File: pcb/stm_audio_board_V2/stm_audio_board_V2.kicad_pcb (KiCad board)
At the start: 4 copper layers, 158 parts, among them J1 Power conn, J10 Conn_01x03_taptempo, J11 SPI, J2 STlink, J3 Audio_sig, J4 Conn_01x10_pots_internal, J6 Conn_01x03_pot_ext, SW1 SW_SPST, U1 STM32H730VBTx, U1 STM32H747IGTx, U2 OP275, U3 STM32H747AIIx, U4 OP275, U5 AMS1117-3.3, U8 L78M09CDT, U9 LF33_TO252, Y1 Crystal_GND24, Y2 X1E0000210132

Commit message: pinsetup ready
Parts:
- removed C13: 2.2uF, Capacitor_SMD:C_0805_2012Metric_Pad1.18x1.45mm_HandSolder
- removed FB1, FB2: FerriteBead, Resistor_SMD:R_0603_1608Metric_Pad0.98x0.95mm_HandSolder
- removed R2: 10k, Resistor_SMD:R_0805_2012Metric_Pad1.20x1.40mm_HandSolder
- removed the U1 at (214.0, 68.3)
- added C103: 2u2F, Capacitor_SMD:C_0603_1608Metric_Pad1.08x0.95mm_HandSolder, F.Cu at (136.3, 102.2)
- added C104: 2u2F, Capacitor_SMD:C_0603_1608Metric_Pad1.08x0.95mm_HandSolder, F.Cu at (136.3, 104.7)
- added C105: 2u2F, Capacitor_SMD:C_0603_1608Metric_Pad1.08x0.95mm_HandSolder, F.Cu at (136.3, 107.3)
- added C3: 10uF 50V ceramic, Capacitor_SMD:C_0603_1608Metric_Pad1.08x0.95mm_HandSolder, F.Cu at (136.3, 92.2)
- added C4: 22uF 50V ceramic, Capacitor_SMD:C_0603_1608Metric_Pad1.08x0.95mm_HandSolder, F.Cu at (136.3, 94.7)
- added C69: 2u2F, Capacitor_SMD:C_0603_1608Metric_Pad1.08x0.95mm_HandSolder, F.Cu at (136.3, 99.7)
- added D1: 1N4148, Diode_THT:D_DO-35_SOD27_P7.62mm_Horizontal, F.Cu at (140.1, 101.0)
- added D2: 1N4148, Diode_THT:D_DO-35_SOD27_P7.62mm_Horizontal, F.Cu at (140.1, 104.5)
- added FB3: TDK MMZ1608R601ATD25 DB, Resistor_SMD:R_0603_1608Metric_Pad0.98x0.95mm_HandSolder, F.Cu at (136.3, 109.8)
- added FB4: TDK MMZ1608R601ATD25 DB, Resistor_SMD:R_0603_1608Metric_Pad0.98x0.95mm_HandSolder, F.Cu at (136.3, 112.3)
- added J5: Conn_01x10_display TODO, Connector_PinHeader_2.54mm:PinHeader_1x10_P2.54mm_Vertical, F.Cu at (129.8, 93.3)
- C15: value 2.2uF -> 2u2F; footprint Capacitor_SMD:C_0805_2012Metric_Pad1.18x1.45mm_HandSolder -> Capacitor_SMD:C_0603_1608Metric_Pad1.08x0.95mm_HandSolder; moved to F.Cu
- U3: value STM32H747AIIx -> MP-K7805-500R3; footprint Package_BGA:UFBGA-169_7x7mm_Layout13x13_P0.5mm -> Package_TO_SOT_THT:TO-220-3_Vertical
- U5: value AMS1117-3.3 -> MIC2920A-3.3WS-TR; footprint Package_TO_SOT_SMD:SOT-223-3_TabPin2 -> Package_TO_SOT_SMD:SOT-223
- U8: value L78M09CDT -> ROHM BA09CC0FP-E2; footprint Package_TO_SOT_SMD:TO-252-2 -> Package_TO_SOT_SMD:TO-252-3_TabPin2
- U9: value LF33_TO252 -> MIC2920A-3.3WS-TR; footprint Package_TO_SOT_SMD:TO-252-2 -> Package_TO_SOT_SMD:SOT-223
- moved C15 85.9 mm to (136.3, 97.2)
- moved U3 52.5 mm to (141.8, 110.2)
- moved U5 48.3 mm to (143.4, 95.1)
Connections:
- C102 pad 1: PWR_INPUT_12V-18V -> 5V
- C15 pad 1: Net-(C15-Pad1) -> 5V
- C27 pad 1: +9V -> Net-(D2-K)
- C28 pad 1: +9V -> Net-(D2-K)
- C48 pad 1: PWR_INPUT_12V-18V -> Net-(D3-K)
- C70 pad 1: Net-(D5-K) -> 5V
- D5 pad 1: Net-(D5-K) -> 5V
- U1 pad 132: SWDIO -> unconnected-(U1-PA13-Pad132)
- U1 pad 138: SWCLK -> unconnected-(U1-PA14-Pad138)
- U1 pad 140: unconnected-(U1-PC10-Pad140) -> AD1939_SPI3_CLK
- U1 pad 141: unconnected-(U1-PC11-Pad141) -> AD1939_SPI3_MISO
- U1 pad 35: unconnected-(U1-PC1-Pad35) -> AD1939_I2S2_SDO
- U1 pad 46: ADC_EN -> unconnected-(U1-PA3-Pad46)
- U1 pad 49: DAC_EN -> AD1939_I2S1_WS
- U1 pad 50: CLK -> AD1939_I2S1_CK
- U1 pad 51: MISO -> AD1939_I2S1_SDI
- U1 pad 52: MOSI -> unconnected-(U1-PA7-Pad52)
- U1 pad 57: unconnected-(U1-PB2-Pad57) -> AD1939_SPI3_MOSI
- U1 pad 78: unconnected-(U1-PB10-Pad78) -> AD1939_I2S2_CK
- U1 pad 85: unconnected-(U1-PB12-Pad85) -> AD1939_I2S2_WS
- U11 pad 20: unconnected-(U11A-DSDATA1-Pad20) -> AD1939_I2S2_SDO
- U11 pad 21: unconnected-(U11A-DBCLK-Pad21) -> AD1939_I2S2_CK
- U11 pad 22: unconnected-(U11A-DLRCLK-Pad22) -> AD1939_I2S2_WS
- U11 pad 27: unconnected-(U11A-ASDATA1-Pad27) -> AD1939_I2S1_SDI
- U11 pad 28: unconnected-(U11A-ABCLK-Pad28) -> AD1939_I2S1_CK
- U11 pad 29: unconnected-(U11A-ALRCLK-Pad29) -> AD1939_I2S1_WS
- U11 pad 30: MOSI -> AD1939_SPI3_MOSI
- U11 pad 31: MISO -> AD1939_SPI3_MISO
- U11 pad 34: CLK -> AD1939_SPI3_CLK
- U11 pad 35: DAC_EN -> AD1939_SPI_CS
- U11 pad 36: unconnected-(U11A-OL1P-Pad36) -> DAC1R
- U11 pad 37: unconnected-(U11A-OL1N-Pad37) -> DAC1L
- U11 pad 38: unconnected-(U11A-OR1P-Pad38) -> DAC2R
- U11 pad 39: unconnected-(U11A-OR1N-Pad39) -> DAC2L
- U11 pad 40: DAC1R -> unconnected-(U11A-OL2P-Pad40)
- U11 pad 41: DAC1L -> unconnected-(U11A-OL2N-Pad41)
- U11 pad 42: DAC2R -> unconnected-(U11A-OR2P-Pad42)
- U11 pad 43: DAC2L -> unconnected-(U11A-OR2N-Pad43)
- U5 pad 1: GND -> Net-(D2-K)
- U5 pad 2: +3.3VA -> GND
- U5 pad 3: +9V -> +3.3VA
- U9 pad 1: Net-(D5-K) -> 5V
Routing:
- net DAC_EN: track 17.3 -> 0.00 mm
- net AD1939_SPI_CS: track 0.00 -> 17.3 mm
- net Net-(D5-K): track 17.1 -> 0.00 mm
- net 5V: track 0.00 -> 17.1 mm
- net (no net): track 0.00 -> 8.78 mm, vias 0 -> 1
- net Net-(C15-Pad1): track 4.45 -> 0.00 mm, vias 1 -> 0
- net Net-(C13-Pad1): track 4.33 -> 0.00 mm

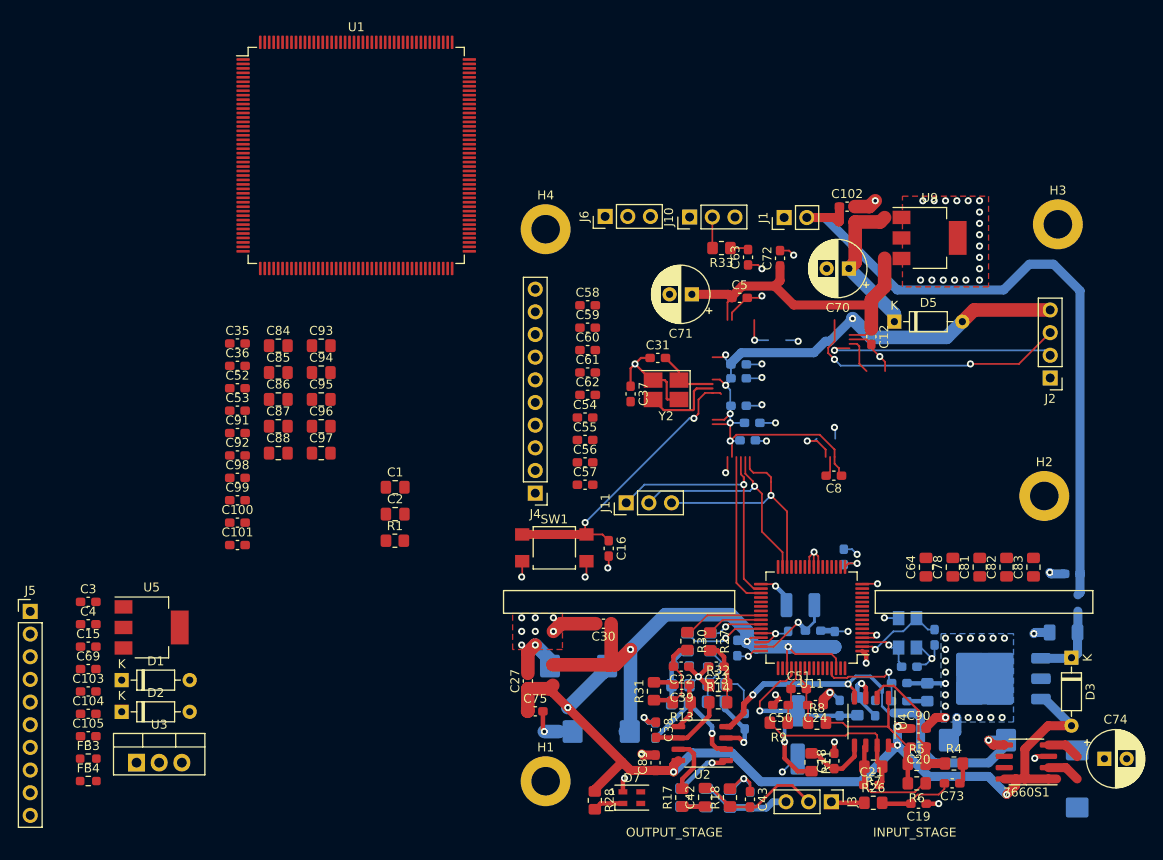
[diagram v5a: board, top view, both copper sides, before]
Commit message: Capacitor types are choosen, schematic updated, unused capacitors deleted. Connectors need to be connected to the mcu and its finished
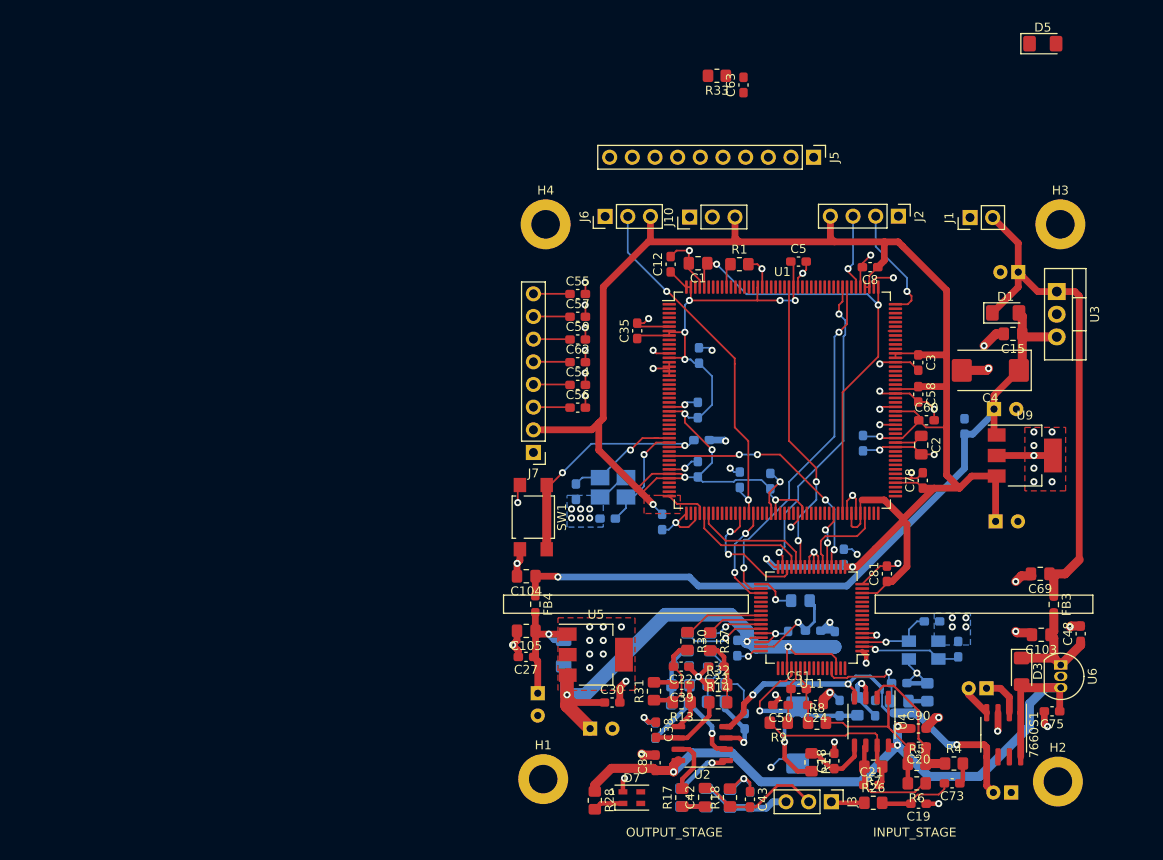
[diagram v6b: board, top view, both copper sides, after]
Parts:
- removed C100, C101, C36, C52, C53, C72, C91, C92, C98, C99: 100nF, Capacitor_SMD:C_0603_1608Metric_Pad1.08x0.95mm_HandSolder
- removed C49: 100uF, Capacitor_SMD:C_1206_3216Metric_Pad1.33x1.80mm_HandSolder
- removed C74: 47uf, Capacitor_THT:CP_Radial_D6.3mm_P2.50mm
- removed C82, C83, C84, C85, C86, C87, C88, C93, C94, C95, C96, C97: 47uF, Capacitor_SMD:C_0805_2012Metric_Pad1.18x1.45mm_HandSolder
- removed J11: SPI, Connector_PinHeader_2.54mm:PinHeader_1x03_P2.54mm_Vertical
- removed J4: Conn_01x10_pots_internal, Connector_PinHeader_2.54mm:PinHeader_1x10_P2.54mm_Vertical
- removed U8: ROHM BA09CC0FP-E2, Package_TO_SOT_SMD:TO-252-3_TabPin2
- added C13: 22uF 50V poly, Capacitor_THT:CP_Radial_D5.0mm_P2.00mm, B.Cu at (240.6, 55.2)
- added J7: Conn_01x8_pots_internal, Connector_PinHeader_2.54mm:PinHeader_1x08_P2.54mm_Vertical, F.Cu at (186.2, 75.5)
- added U6: L7809, Package_TO_SOT_THT:TO-92_Inline, F.Cu at (245.3, 99.3)
- C102, C16, C31, C37, C61, C70, C71, Y2: moved to B.Cu
- C103, C104, C105, C15, C67, C69: footprint Capacitor_SMD:C_0603_1608Metric_Pad1.08x0.95mm_HandSolder -> Capacitor_SMD:C_0805_2012Metric_Pad1.18x1.45mm_HandSolder
- C26: value 100uF -> 100uF tantal; footprint Capacitor_SMD:CP_Elec_6.3x7.7 -> Capacitor_Tantalum_SMD:CP_EIA-7343-31_Kemet-D_Pad2.25x2.55mm_HandSolder
- C28: footprint Capacitor_Tantalum_SMD:CP_EIA-7343-31_Kemet-D_Pad2.25x2.55mm_HandSolder -> Capacitor_THT:CP_Radial_D6.3mm_P2.50mm
- C29: value 1uF -> 47uF; footprint Capacitor_Tantalum_SMD:CP_EIA-7343-31_Kemet-D_Pad2.25x2.55mm_HandSolder -> Capacitor_THT:CP_Radial_D6.3mm_P2.50mm
- C3: value 10uF 50V ceramic -> 100nF
- C4: value 22uF 50V ceramic -> 22uF tantal; footprint Capacitor_SMD:C_0603_1608Metric_Pad1.08x0.95mm_HandSolder -> Capacitor_Tantalum_SMD:CP_EIA-7343-31_Kemet-D_Pad2.25x2.55mm_HandSolder
- C48: moved to F.Cu
- C64: value 47uF -> 100nF; footprint Capacitor_SMD:C_0805_2012Metric_Pad1.18x1.45mm_HandSolder -> Capacitor_SMD:C_0603_1608Metric_Pad1.08x0.95mm_HandSolder; moved to B.Cu
- C76, C77: footprint Capacitor_Tantalum_SMD:CP_EIA-7343-31_Kemet-D_Pad2.25x2.55mm_HandSolder -> Capacitor_THT:CP_Radial_D5.0mm_P2.00mm
- C78, C81: value 47uF -> 100nF; footprint Capacitor_SMD:C_0805_2012Metric_Pad1.18x1.45mm_HandSolder -> Capacitor_SMD:C_0603_1608Metric_Pad1.08x0.95mm_HandSolder
- C80: value 10uF -> 10uF tantal; footprint Capacitor_SMD:C_1210_3225Metric_Pad1.33x2.70mm_HandSolder -> Capacitor_SMD:C_0805_2012Metric_Pad1.18x1.45mm_HandSolder
- D1, D3, D5: footprint Diode_THT:D_DO-35_SOD27_P7.62mm_Horizontal -> Diode_SMD:D_1206_3216Metric_Pad1.42x1.75mm_HandSolder
- D2: footprint Diode_THT:D_DO-35_SOD27_P7.62mm_Horizontal -> Diode_SMD:D_1206_3216Metric_Pad1.42x1.75mm_HandSolder; moved to B.Cu
- J5: value Conn_01x10_display TODO -> Conn_01x10_display
- U5, U9: footprint Package_TO_SOT_SMD:SOT-223 -> Package_TO_SOT_SMD:SOT-223-3_TabPin2
- moved U3 115.9 mm to (244.9, 57.4), turned to -90 degrees
- moved FB3 109.6 mm to (244.5, 92.5), turned to -90 degrees
- moved C15 109.4 mm to (240.0, 62.2), turned to 180 degrees
- moved D1 107.3 mm to (239.2, 59.8)
- moved C69 107.2 mm to (243.0, 89.1), turned to 180 degrees
- moved C103 107.0 mm to (243.1, 95.9), turned to 180 degrees
- moved C4 105.0 mm to (237.4, 66.3), turned to 180 degrees
- moved J5 101.5 mm to (217.6, 42.4), turned to -90 degrees
- moved C3 96.8 mm to (229.4, 65.4), turned to -90 degrees
- moved C2 59.5 mm to (229.7, 74.6), turned to -90 degrees
- moved C75 57.9 mm to (244.3, 104.5), turned to 180 degrees
- moved U1 55.1 mm to (214.1, 69.6)
- moved FB4 53.9 mm to (186.4, 92.5), turned to -90 degrees
- moved C104 51.5 mm to (185.4, 89.3), turned to 180 degrees
- moved C105 50.5 mm to (185.4, 95.5), turned to 180 degrees
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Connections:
- C3 pad 1: PWR_INPUT_12V-18V -> +3.3V
- C35 pad 1: +3.3VA -> +3.3V
- C58 pad 1: POT7 -> +3.3V
- C60 pad 1: POT8 -> +3.3V
- C64 pad 1: +3.3VA -> +3.3V
- C78 pad 1: +3.3VA -> +3.3V
- C81 pad 1: +3.3VA -> +3.3V
- J10 pad 3: VDD -> +3.3V
- J5 pad 1: unconnected-(J5-Pin_1-Pad1) -> +3.3V
- J5 pad 10: unconnected-(J5-Pin_10-Pad10) -> TOUCH_IRQ
- J5 pad 2: unconnected-(J5-Pin_2-Pad2) -> GND
- J5 pad 3: unconnected-(J5-Pin_3-Pad3) -> DISPLAY_CS
- J5 pad 4: unconnected-(J5-Pin_4-Pad4) -> DISPLAY_RST
- J5 pad 5: unconnected-(J5-Pin_5-Pad5) -> DISPLAY_DC
- J5 pad 6: unconnected-(J5-Pin_6-Pad6) -> DISPLAY_MOSI
- J5 pad 7: unconnected-(J5-Pin_7-Pad7) -> DISPLAY_SCK
- J5 pad 8: unconnected-(J5-Pin_8-Pad8) -> DISPLAY_MISO
- J5 pad 9: unconnected-(J5-Pin_9-Pad9) -> TOUCH_CS
- J6 pad 3: VDD -> +3.3V
- U1 pad 1: unconnected-(U1-PE2-Pad1) -> DISPLAY_SCK
- U1 pad 118: unconnected-(U1-PG8-Pad118) -> EXT_INT_BUTTON
- U1 pad 132: unconnected-(U1-PA13-Pad132) -> SWDIO
- U1 pad 138: unconnected-(U1-PA14-Pad138) -> SWCLK
- U1 pad 153: unconnected-(U1-PG9-Pad153) -> AD1939_I2S1_SDI
- U1 pad 169: unconnected-(U1-PB9-Pad169) -> TOUCH_IRQ
- U1 pad 170: unconnected-(U1-PE0-Pad170) -> DISPLAY_RST
- U1 pad 171: unconnected-(U1-PE1-Pad171) -> TOUCH_CS
- U1 pad 2: unconnected-(U1-PE3-Pad2) -> DISPLAY_CS
- U1 pad 3: unconnected-(U1-PE4-Pad3) -> DISPLAY_DC
- U1 pad 34: unconnected-(U1-PC0-Pad34) -> POT4
- U1 pad 4: unconnected-(U1-PE5-Pad4) -> DISPLAY_MISO
- U1 pad 5: unconnected-(U1-PE6-Pad5) -> DISPLAY_MOSI
- U1 pad 51: AD1939_I2S1_SDI -> POT1
- U1 pad 52: unconnected-(U1-PA7-Pad52) -> POT2
- U1 pad 54: unconnected-(U1-PC5-Pad54) -> POT5
- U1 pad 56: unconnected-(U1-PB1-Pad56) -> POT3
- U1 pad 58: unconnected-(U1-PF11-Pad58) -> POT6
- U1 pad 59: unconnected-(U1-PF12-Pad59) -> POT_EXT
- U1 pad 60: unconnected-(U1-PF13-Pad60) -> AD1939_SPI_CS
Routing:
- net +3.3V: track 119.5 -> 302.8 mm, vias 7 -> 13
- net 5V: track 17.1 -> 84.1 mm, vias 0 -> 1
- net GND: track 152.7 -> 215.0 mm, vias 86 -> 88
- net Net-(C1-Pad1): track 0.00 -> 50.9 mm, vias 0 -> 2
- net POT_EXT: track 0.00 -> 40.8 mm, vias 0 -> 2
- net AD1939_SPI3_CLK: track 0.00 -> 40.3 mm, vias 0 -> 2
- net AD1939_SPI3_MISO: track 0.00 -> 35.0 mm, vias 0 -> 2
- net AD1939_I2S1_SDI: track 0.00 -> 33.6 mm, vias 0 -> 2
- net CLK: track 31.0 -> 0.00 mm, vias 1 -> 0
- net AD1939_I2S2_SDO: track 0.00 -> 27.7 mm, vias 0 -> 4
- net MISO: track 26.7 -> 0.00 mm, vias 1 -> 0
- net MOSI: track 26.4 -> 0.00 mm, vias 1 -> 0
- net SWCLK: track 31.0 -> 8.54 mm, vias 2 -> 1
- net +9V: track 106.8 -> 86.5 mm, vias 5 -> 3
- net PWR_INPUT_12V-18V: track 76.1 -> 57.3 mm
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- added copper zone on F.Cu, net +3.3V
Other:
- board text removed: "U8"

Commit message: pcb seems to be finished drc error: 0
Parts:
- removed J10: Conn_01x03_taptempo, Connector_PinHeader_2.54mm:PinHeader_1x03_P2.54mm_Vertical
- added J4: Conn_01x01_taptempo, Connector_PinHeader_2.54mm:PinHeader_1x01_P2.54mm_Vertical, F.Cu at (232.5, 49.1)
- C31, C37, Y2: moved to F.Cu
- C54, C55, C56, C57, C59, C62, C63, R33: moved to B.Cu
- moved D5 45.8 mm to (234.9, 74.7), turned to -90 degrees
- moved R33 36.8 mm to (222.7, 66.4)
- moved C63 36.5 mm to (222.7, 68.3), turned to 180 degrees
- moved J6 36.5 mm to (186.2, 84.6), turned to 180 degrees
- moved J5 25.8 mm to (192.7, 49.0), turned to 90 degrees
- moved C31 10.1 mm to (197.7, 72.2)
- moved SW1 9.21 mm to (195.0, 85.6), turned to 0 degrees
- moved C37 7.97 mm to (197.7, 75.5), turned to -90 degrees
- moved C61 7.89 mm to (207.3, 70.9)
- moved Y2 5.66 mm to (194.5, 73.7), turned to -90 degrees
- moved J1 2.03 mm to (237.2, 49.1)
- moved C104 1.02 mm to (186.4, 89.3)
- moved C54 1.02 mm to (190.2, 67.9)
- moved C56 1.02 mm to (190.2, 70.4)
- moved C59 1.02 mm to (190.2, 62.8)
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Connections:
- U1 pad 21: unconnected-(U1-PF3-Pad21) -> POT1
- U1 pad 23: unconnected-(U1-PF5-Pad23) -> POT2
- U1 pad 26: unconnected-(U1-PF6-Pad26) -> POT3
- U1 pad 27: unconnected-(U1-PF7-Pad27) -> POT4
- U1 pad 28: unconnected-(U1-PF8-Pad28) -> POT5
- U1 pad 29: unconnected-(U1-PF9-Pad29) -> POT6
- U1 pad 30: unconnected-(U1-PF10-Pad30) -> POT_EXT
- U1 pad 34: POT4 -> unconnected-(U1-PC0-Pad34)
- U1 pad 51: POT1 -> unconnected-(U1-PA6-Pad51)
- U1 pad 52: POT2 -> unconnected-(U1-PA7-Pad52)
- U1 pad 54: POT5 -> unconnected-(U1-PC5-Pad54)
- U1 pad 56: POT3 -> unconnected-(U1-PB1-Pad56)
- U1 pad 58: POT6 -> unconnected-(U1-PF11-Pad58)
- U1 pad 59: POT_EXT -> unconnected-(U1-PF12-Pad59)
- U11 pad 19: unconnected-(U11A-DSDATA2-Pad19) -> AD1939_I2S2_SDO
- U11 pad 20: AD1939_I2S2_SDO -> unconnected-(U11A-DSDATA1-Pad20)
- U11 pad 36: DAC1R -> unconnected-(U11A-OL1P-Pad36)
- U11 pad 37: DAC1L -> unconnected-(U11A-OL1N-Pad37)
- U11 pad 38: DAC2R -> unconnected-(U11A-OR1P-Pad38)
- U11 pad 39: DAC2L -> unconnected-(U11A-OR1N-Pad39)
- U11 pad 40: unconnected-(U11A-OL2P-Pad40) -> DAC1R
- U11 pad 41: unconnected-(U11A-OL2N-Pad41) -> DAC1L
- U11 pad 42: unconnected-(U11A-OR2P-Pad42) -> DAC2R
- U11 pad 43: unconnected-(U11A-OR2N-Pad43) -> DAC2L
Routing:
- net +3.3V: track 302.8 -> 332.8 mm, vias 13 -> 15
- net GND: track 215.0 -> 237.2 mm, vias 88 -> 92
- net DISPLAY_MISO: track 0.00 -> 22.1 mm, vias 0 -> 1
- net TAP_TEMPO_INPUT: track 0.00 -> 21.8 mm
- net POT1: track 4.11 -> 23.6 mm, vias 0 -> 1
- net DISPLAY_MOSI: track 0.00 -> 19.2 mm
- net DISPLAY_DC: track 0.00 -> 18.3 mm, vias 0 -> 1
- net DISPLAY_SCK: track 0.00 -> 18.3 mm, vias 0 -> 1
- net POT2: track 4.11 -> 20.4 mm, vias 0 -> 1
- net POT3: track 4.12 -> 18.8 mm, vias 0 -> 1
- net POT4: track 4.12 -> 18.6 mm, vias 0 -> 1
- net POT_EXT: track 40.8 -> 27.2 mm
- net DISPLAY_RST: track 0.00 -> 13.4 mm, vias 0 -> 1
- net TOUCH_IRQ: track 0.00 -> 13.0 mm
- net DISPLAY_CS: track 0.00 -> 13.0 mm, vias 0 -> 1
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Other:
- board outline added: 66 x 71.1 mm
- board text removed: "INPUT_STAGE"
- board text removed: "OUTPUT_STAGE"

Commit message: Update stm_audio_board_V2-B_Cu.gbr, stm_audio_board_V2-B_Mask.gbr, and 14 more files...
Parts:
- C15, C4, D1: moved to B.Cu
- moved C13 4.10 mm to (236.5, 54.7)
- moved U3 3.05 mm to (244.9, 60.5)
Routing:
- net PWR_INPUT_12V-18V: track 56.5 -> 64.2 mm
- net GND: track 237.2 -> 234.9 mm, vias 92 -> 115
- net 5V: track 86.9 -> 88.0 mm
